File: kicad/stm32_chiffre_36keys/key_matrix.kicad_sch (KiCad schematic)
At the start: 81 parts, among them SW1 SW_Push, SW10 SW_Push, SW11 SW_Push, SW12 SW_Push, SW13 SW_Push, SW14 SW_Push, SW15 SW_Push, SW16 SW_Push, SW17 SW_Push, SW18 SW_Push, SW19 SW_Push, SW2 SW_Push, SW20 SW_Push, SW21 SW_Push, SW22 SW_Push, SW23 SW_Push, SW24 SW_Push, SW25 SW_Push, SW26 SW_Push, SW27 SW_Push, SW28 SW_Push, SW29 SW_Push, SW3 SW_Push, SW30 SW_Push, SW31 SW_Push, SW32 SW_Push, SW33 SW_Push, SW34 SW_Push, SW35 SW_Push, SW36 Rotary_Encoder_Switch, SW38 SW_Push, SW39 SW_Push, SW4 SW_Push, SW40 SW_Push, SW41 SW_Push, SW42 SW_Push, SW43 SW_Push, SW5 SW_Push, SW6 SW_Push, SW7 SW_Push, SW8 SW_Push, SW9 SW_Push

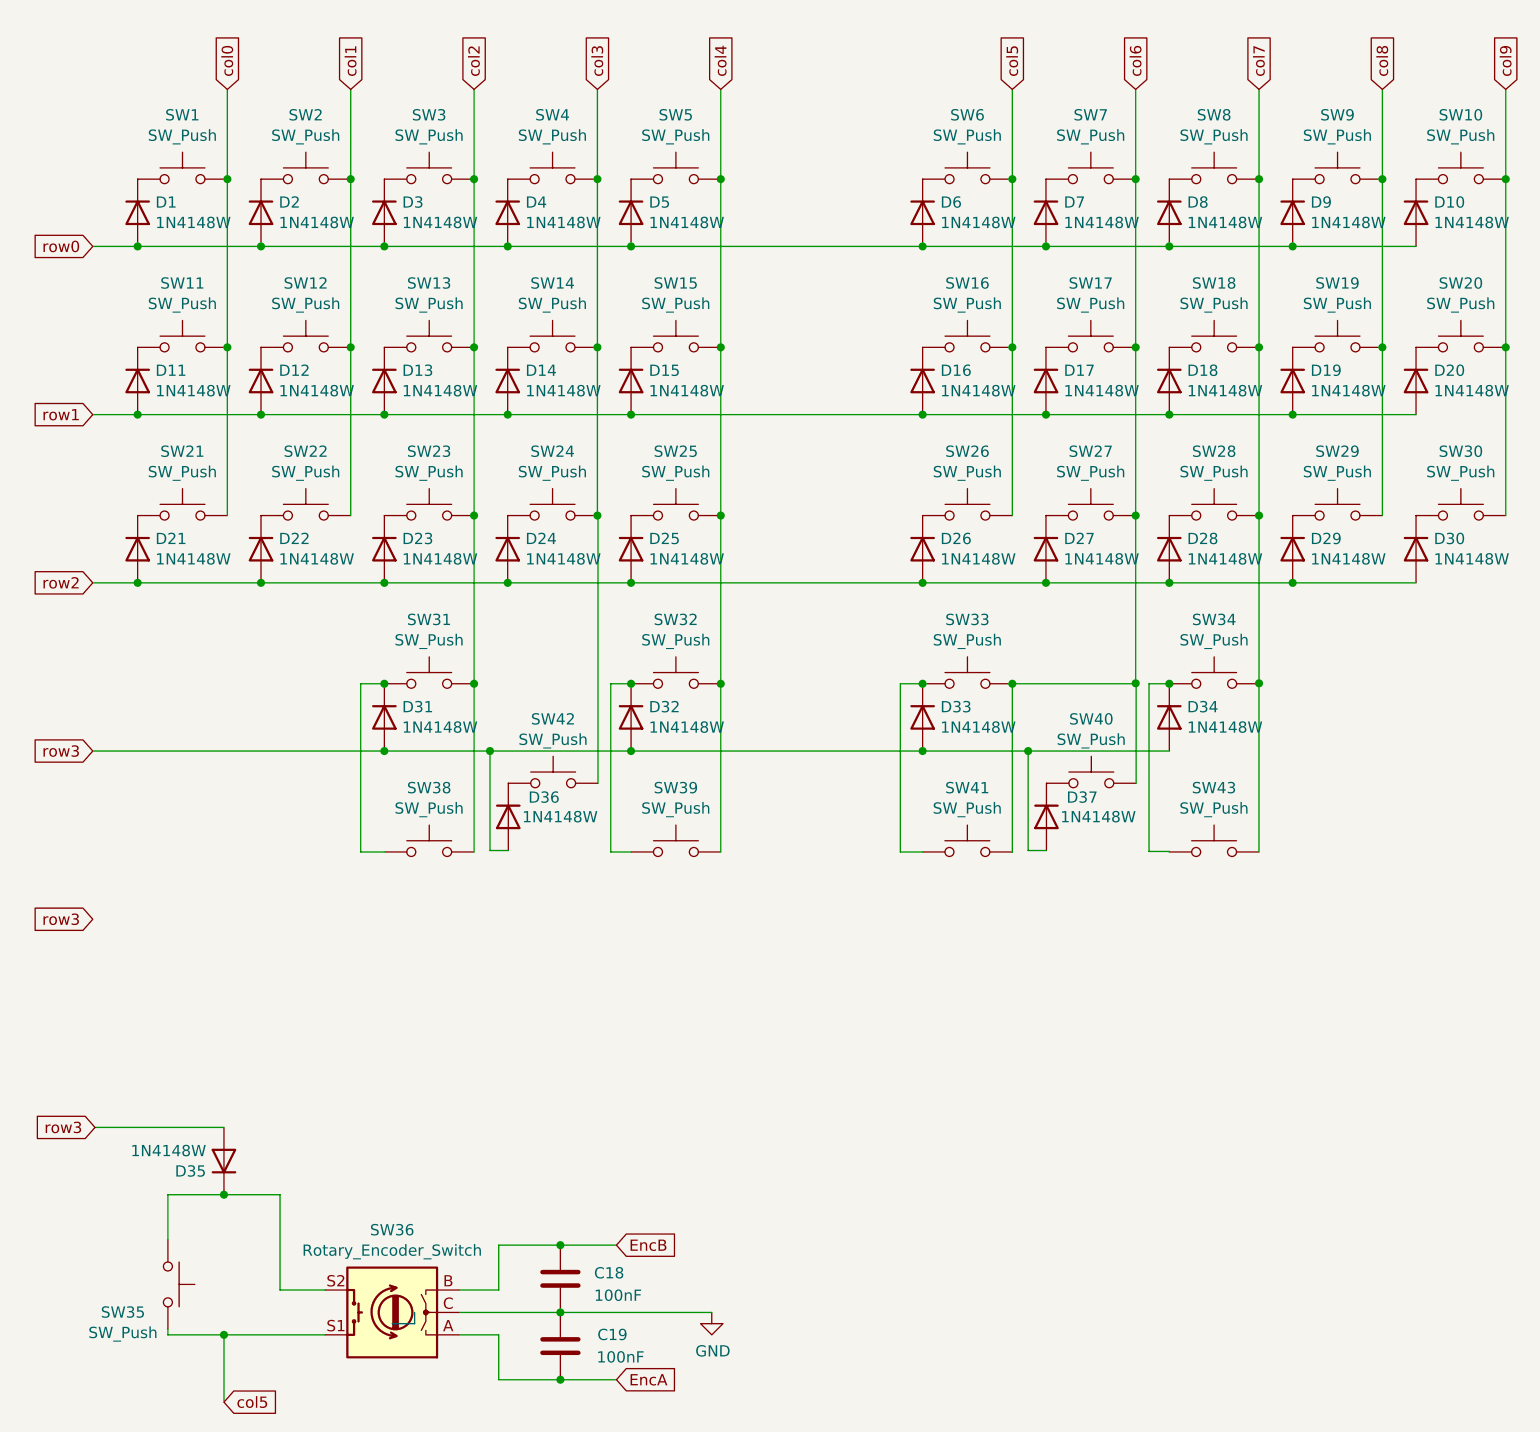
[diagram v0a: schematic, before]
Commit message: fix schematic on right thumb keys
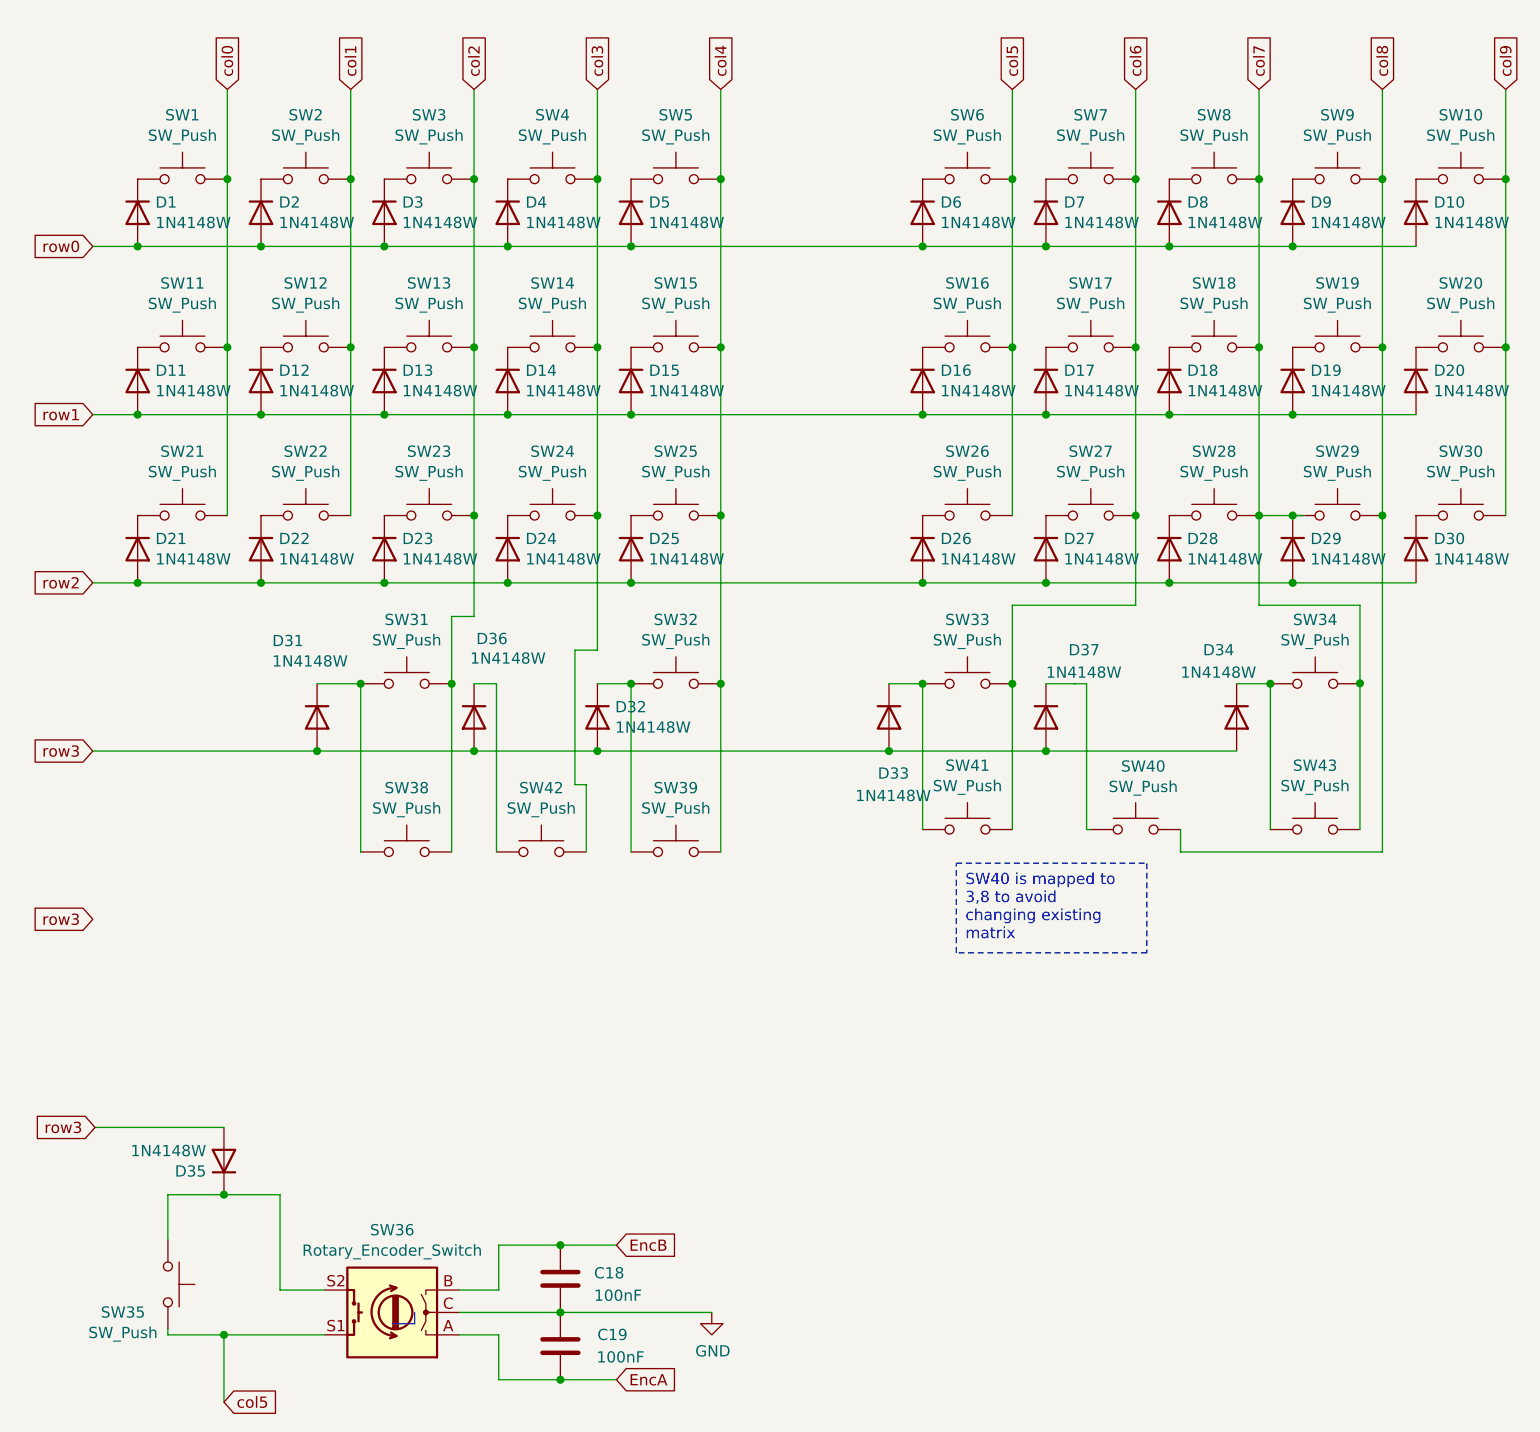
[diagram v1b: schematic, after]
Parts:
- D37: JlcRotOffset 14 -> -14
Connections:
- net col6: no longer SW40.2
- net col7: now also D29.1 (K), SW29.1
- net col8: now also SW40.2
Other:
- title: Hotswap Chiffre -> Hotswap Chiffre (36 key)
- moved on the sheet: D31, D32, D33, D36, SW31, SW34, SW38, SW40, SW41, SW42, SW43
